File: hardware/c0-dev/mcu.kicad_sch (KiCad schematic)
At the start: 28 parts, among them J2 TAG_CONNECT, U7 W25Q128JVP, U8 RP2350A, Y1 ABM8-272-T3 (12Mhz)

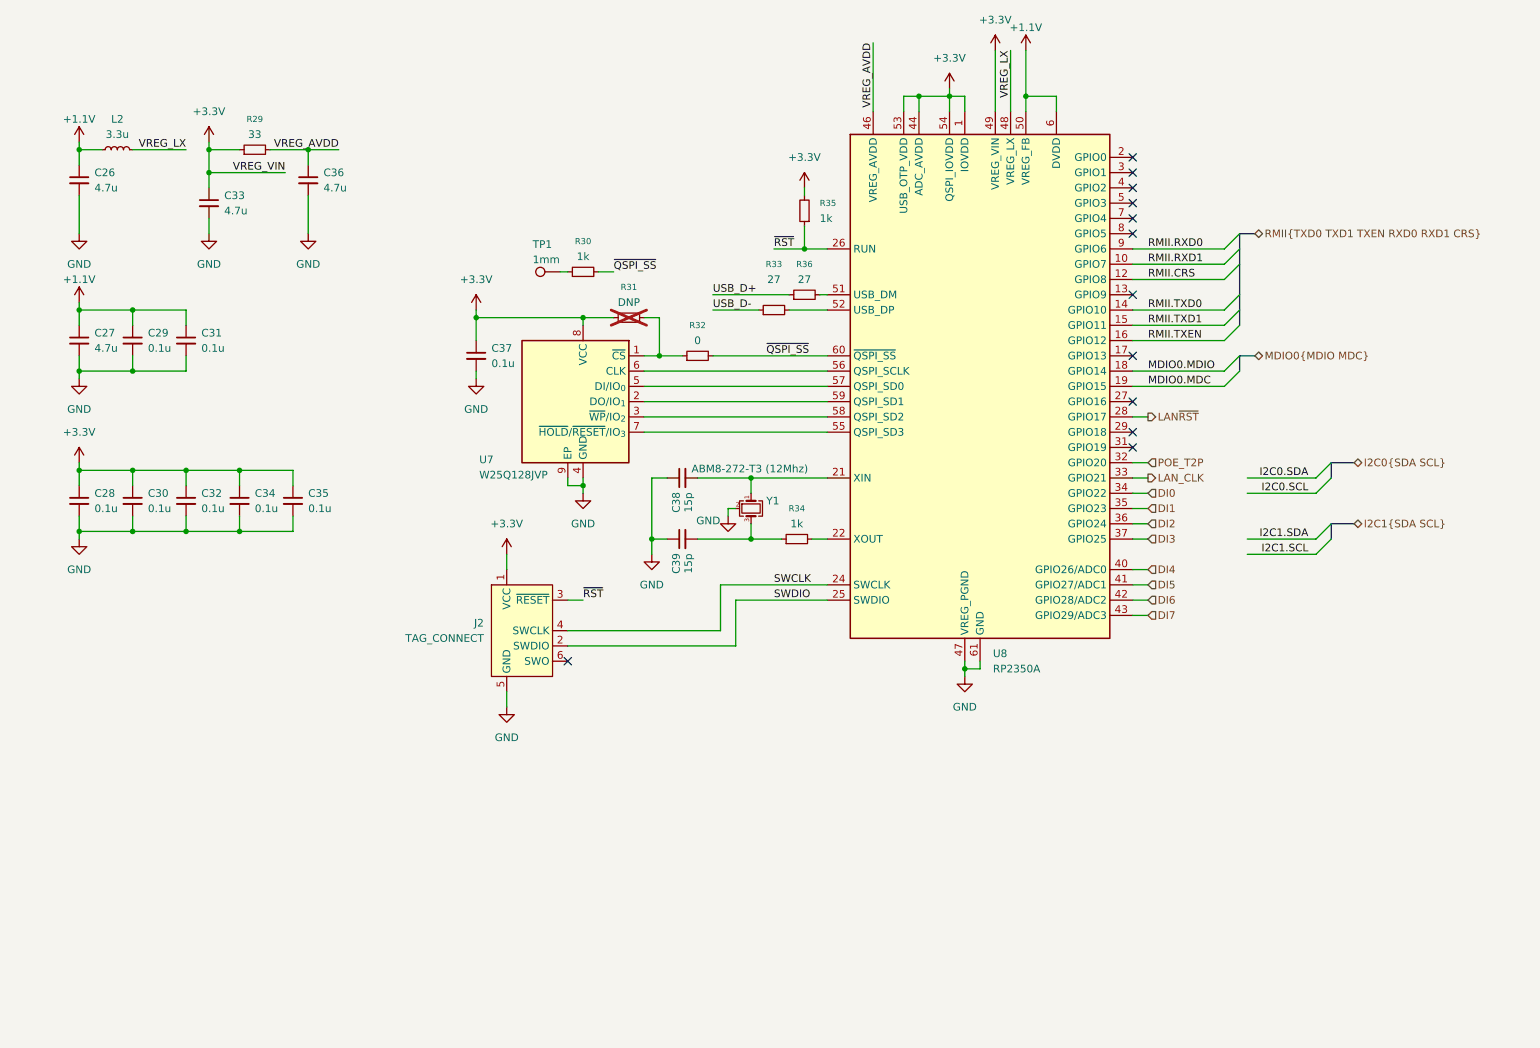
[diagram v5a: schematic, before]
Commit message: connections and i2c clock split
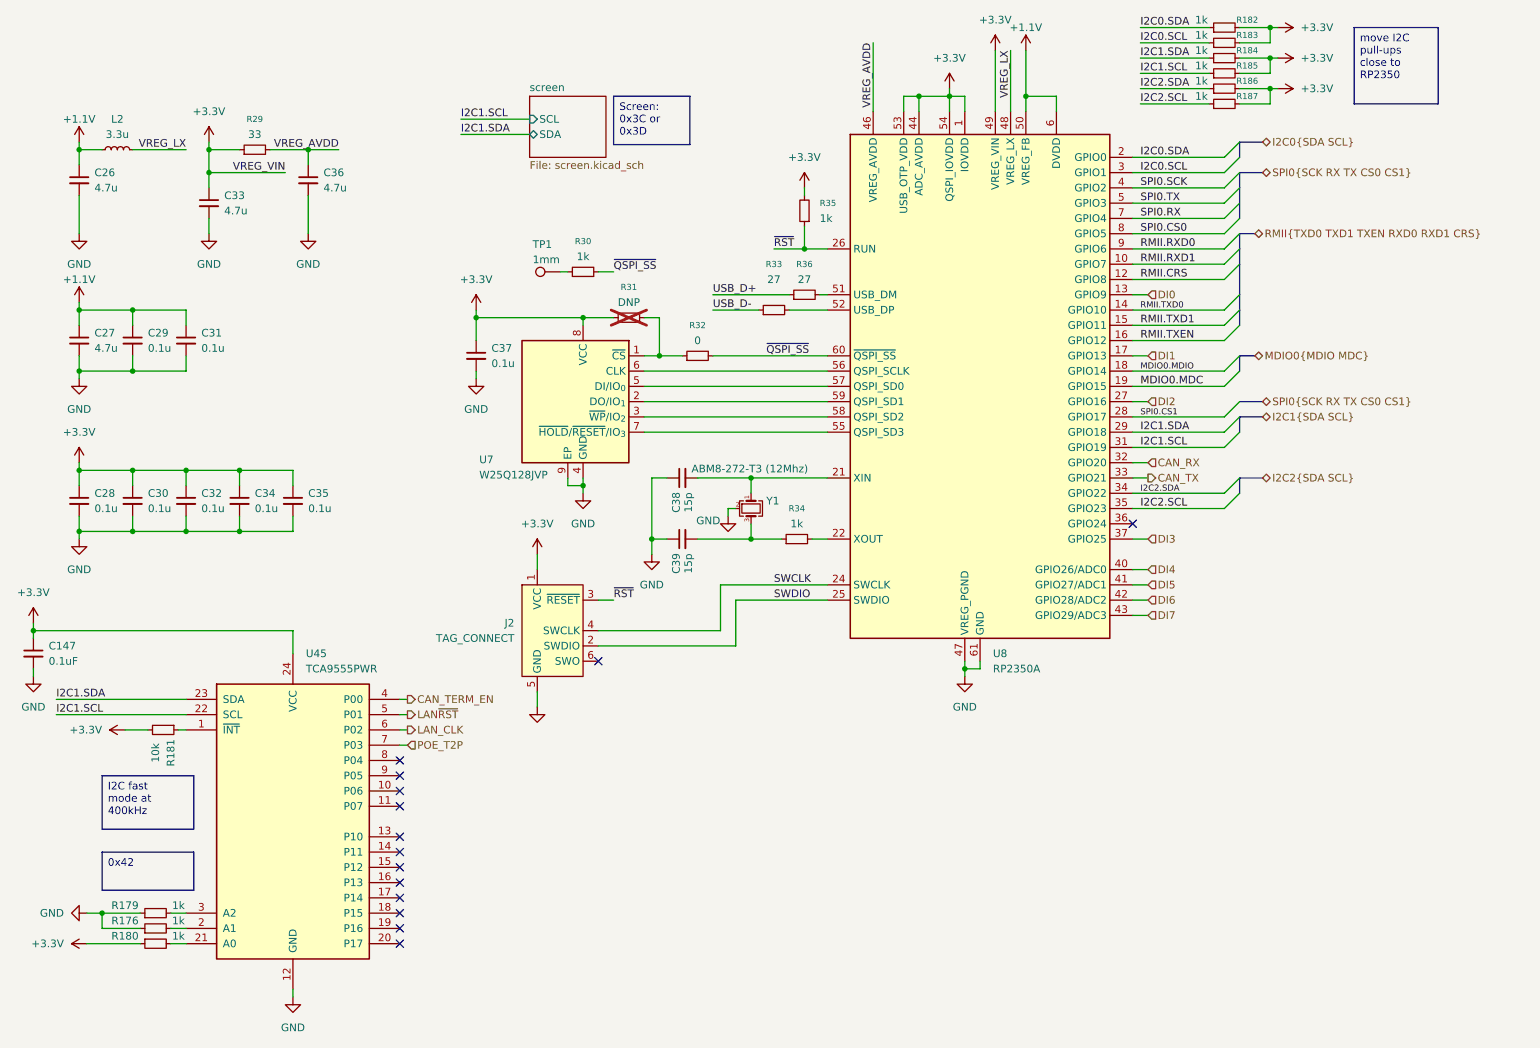
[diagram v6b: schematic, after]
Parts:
- added C147: 0.1uF, Capacitor_SMD:C_0402_1005Metric, symbol Device:C_Small
- added R176, R179, R180, R182, R183, R184, R185, R186, R187: 1k, Resistor_SMD:R_0402_1005Metric, symbol Device:R_Small
- added R181: 10k, Resistor_SMD:R_0402_1005Metric, symbol Device:R_Small
- added U45: TCA9555PWR, Package_SO:TSSOP-24_4.4x7.8mm_P0.65mm, symbol Interface_Expansion:TCA9555PWR
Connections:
- net +3.3V: now also C147.1, R180.1, R181.2, R182.2, R183.2, R184.2, R185.2, R186.2, R187.2, U45.24 (VCC)
- net DI0: now also U8.13 (GPIO9); no longer U8.34 (GPIO22)
- net DI1: now also U8.17 (GPIO13); no longer U8.35 (GPIO23)
- net DI2: now also U8.27 (GPIO16); no longer U8.36 (GPIO24)
- net GND: now also C147.2, R176.1, R179.1, U45.12 (GND)
- net I2C0.SCL: now also U8.3 (GPIO1), R183.1
- net I2C0.SDA: now also U8.2 (GPIO0), R182.1
- net I2C1.SCL: now also U8.31 (GPIO19), R185.1, U45.22 (SCL)
- net I2C1.SDA: now also U8.29 (GPIO18), R184.1, U45.23 (SDA)
- net LAN_CLK: now also U45.6 (P02); no longer U8.33 (GPIO21)
- net LAN~{RST}: now also U45.5 (P01); no longer U8.28 (GPIO17)
- net POE_T2P: now also U45.7 (P03); no longer U8.32 (GPIO20)
- net SPI0.SCK: now reaches U8.4 (GPIO2)
- net SPI0.TX: now reaches U8.5 (GPIO3)
- net SPI0.RX: now reaches U8.7 (GPIO4)
- net SPI0.CS0: now reaches U8.8 (GPIO5)
- new net: R181.1, U45.1 (~{INT})
- new net: R176.2, U45.2 (A1)
- new net: R180.2, U45.21 (A0)
- new net: R179.2, U45.3 (A2)
- new net CAN_RX: U8.32 (GPIO20)
- new net CAN_TERM_EN: U45.4 (P00)
- new net CAN_TX: U8.33 (GPIO21)
- new net I2C2.SCL: R187.1, U8.35 (GPIO23)
- new net I2C2.SDA: R186.1, U8.34 (GPIO22)
- new net SPI0.CS1: U8.28 (GPIO17)
- no-connect marks 12 -> 14
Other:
- added sheet screen (screen.kicad_sch)
- moved on the sheet: J2

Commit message: connector
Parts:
- added TP2, TP3: TestPoint, TestPoint:TestPoint_Pad_D2.0mm, symbol Connector:TestPoint
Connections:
- net USB_D+: now also TP2.1
- net USB_D-: now also TP3.1
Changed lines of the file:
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@@
 	(wire
 		(pts
+			(xy 259.08 135.89) (xy 259.08 139.7)
+		)
+		(stroke
+			(width 0)
+			(type default)
+		)
+	)
+	(wire
+		(pts
 			(xy 218.44 44.45) (xy 233.68 44.45)
 		)
@@
 	(wire
 		(pts
+			(xy 247.65 135.89) (xy 259.08 135.89)
+		)
+		(stroke
+			(width 0)
+			(type default)
+		)
+	)
+	(wire
+		(pts
 			(xy 58.42 175.26) (xy 60.96 175.26)
 		)
@@
 	(wire
 		(pts
+			(xy 247.65 133.35) (xy 260.35 133.35)
+		)
+		(stroke
+			(width 0)
+			(type default)
+		)
+	)
+	(wire
+		(pts
 			(xy 218.44 107.95) (xy 220.98 107.95)
 		)
@@
 	(wire
 		(pts
+			(xy 259.08 139.7) (xy 260.35 139.7)
+		)
+		(stroke
+			(width 0)
+			(type default)
+		)
+	)
+	(wire
+		(pts
 			(xy 64.77 41.91) (xy 64.77 43.18)
 		)
@@
 		)
 	)
+	(label "USB_D-"
+		(at 247.65 135.89 0)
+		(effects
+			(font
+				(size 1.27 1.27)
+			)
+			(justify left bottom)
+		)
+	)
 	(label "VREG_LX"
 		(at 60.96 43.18 180)
@@
 		)
 	)
+	(label "USB_D+"
+		(at 247.65 133.35 0)
+		(effects
+			(font
+				(size 1.27 1.27)
+			)
+			(justify left bottom)
+		)
+	)
 	(label "SPI0.TX"
 		(at 219.71 52.07 0)
@@
 	)
 	(symbol
+		(lib_id "Connector:TestPoint")
+		(at 260.35 139.7 270)
+		(unit 1)
+		(body_style 1)
+		(exclude_from_sim no)
+		(in_bom yes)
+		(on_board yes)
+		(in_pos_files yes)
+		(dnp no)
+		(fields_autoplaced yes)
+		(property "Reference" "TP3"
+			(at 265.43 138.4299 90)
+			(show_name no)
+			(do_not_autoplace no)
+			(effects
+				(font
+					(size 1.27 1.27)
+				)
+				(justify left)
+			)
+		)
+		(property "Value" "TestPoint"
+			(at 265.43 140.9699 90)
+			(show_name no)
+			(do_not_autoplace no)
+			(effects
+				(font
+					(size 1.27 1.27)
+				)
+				(justify left)
+			)
+		)
+		(property "Footprint" "TestPoint:TestPoint_Pad_D2.0mm"
+			(at 260.35 144.78 0)
+			(hide yes)
+			(show_name no)
+			(do_not_autoplace no)
+			(effects
+				(font
+					(size 1.27 1.27)
+				)
+			)
+		)
+		(property "Datasheet" ""
+			(at 260.35 144.78 0)
+			(hide yes)
+			(show_name no)
+			(do_not_autoplace no)
+			(effects
+				(font
+					(size 1.27 1.27)
+				)
+			)
+		)
+		(property "Description" "test point"
+			(at 260.35 139.7 0)
+			(hide yes)
+			(show_name no)
+			(do_not_autoplace no)
+			(effects
+				(font
+					(size 1.27 1.27)
+				)
+			)
+		)
+		(pin "1"
+		)
+		(instances
+			(project "c0-dev"
+				(path "/b8347a0e-ad04-4414-969d-3c64a611d74e/b3a362d3-bb15-48bf-a1e5-1773c27a02b7"
+					(reference "TP3")
+					(unit 1)
+				)
+			)
+		)
+	)
+	(symbol
 		(lib_id "Device:C_Small")
 		(at 35.56 127 0)
@@
 					(unit 1)
 				)
+			)
+		)
+	)
+	(symbol
+		(lib_id "Connector:TestPoint")
+		(at 260.35 133.35 270)
+		(unit 1)
+		(body_style 1)
+		(exclude_from_sim no)
+		(in_bom yes)
+		(on_board yes)
+		(in_pos_files yes)
+		(dnp no)
+		(fields_autoplaced yes)
+		(property "Reference" "TP2"
+			(at 265.43 132.0799 90)
+			(show_name no)
+			(do_not_autoplace no)
+			(effects
+				(font
+					(size 1.27 1.27)
+				)
+				(justify left)
+			)
+		)
+		(property "Value" "TestPoint"
+			(at 265.43 134.6199 90)
+			(show_name no)
+			(do_not_autoplace no)
+			(effects
+				(font
+					(size 1.27 1.27)
+				)
+				(justify left)
+			)
+		)
+		(property "Footprint" "TestPoint:TestPoint_Pad_D2.0mm"
+			(at 260.35 138.43 0)
+			(hide yes)
+			(show_name no)
+			(do_not_autoplace no)
+			(effects
+				(font
+					(size 1.27 1.27)
+				)
+			)
+		)
+		(property "Datasheet" ""
+			(at 260.35 138.43 0)
+			(hide yes)
+			(show_name no)
+			(do_not_autoplace no)
+			(effects
+				(font
+					(size 1.27 1.27)
+				)
+			)
+		)
+		(property "Description" "test point"
+			(at 260.35 133.35 0)
+			(hide yes)
+			(show_name no)
+			(do_not_autoplace no)
+			(effects
+				(font
+					(size 1.27 1.27)
+				)
+			)
+		)
+		(pin "1"
+		)
+		(instances
+			(project "c0-dev"
+				(path "/b8347a0e-ad04-4414-969d-3c64a611d74e/b3a362d3-bb15-48bf-a1e5-1773c27a02b7"
+					(reference "TP2")
+					(unit 1)
+				)

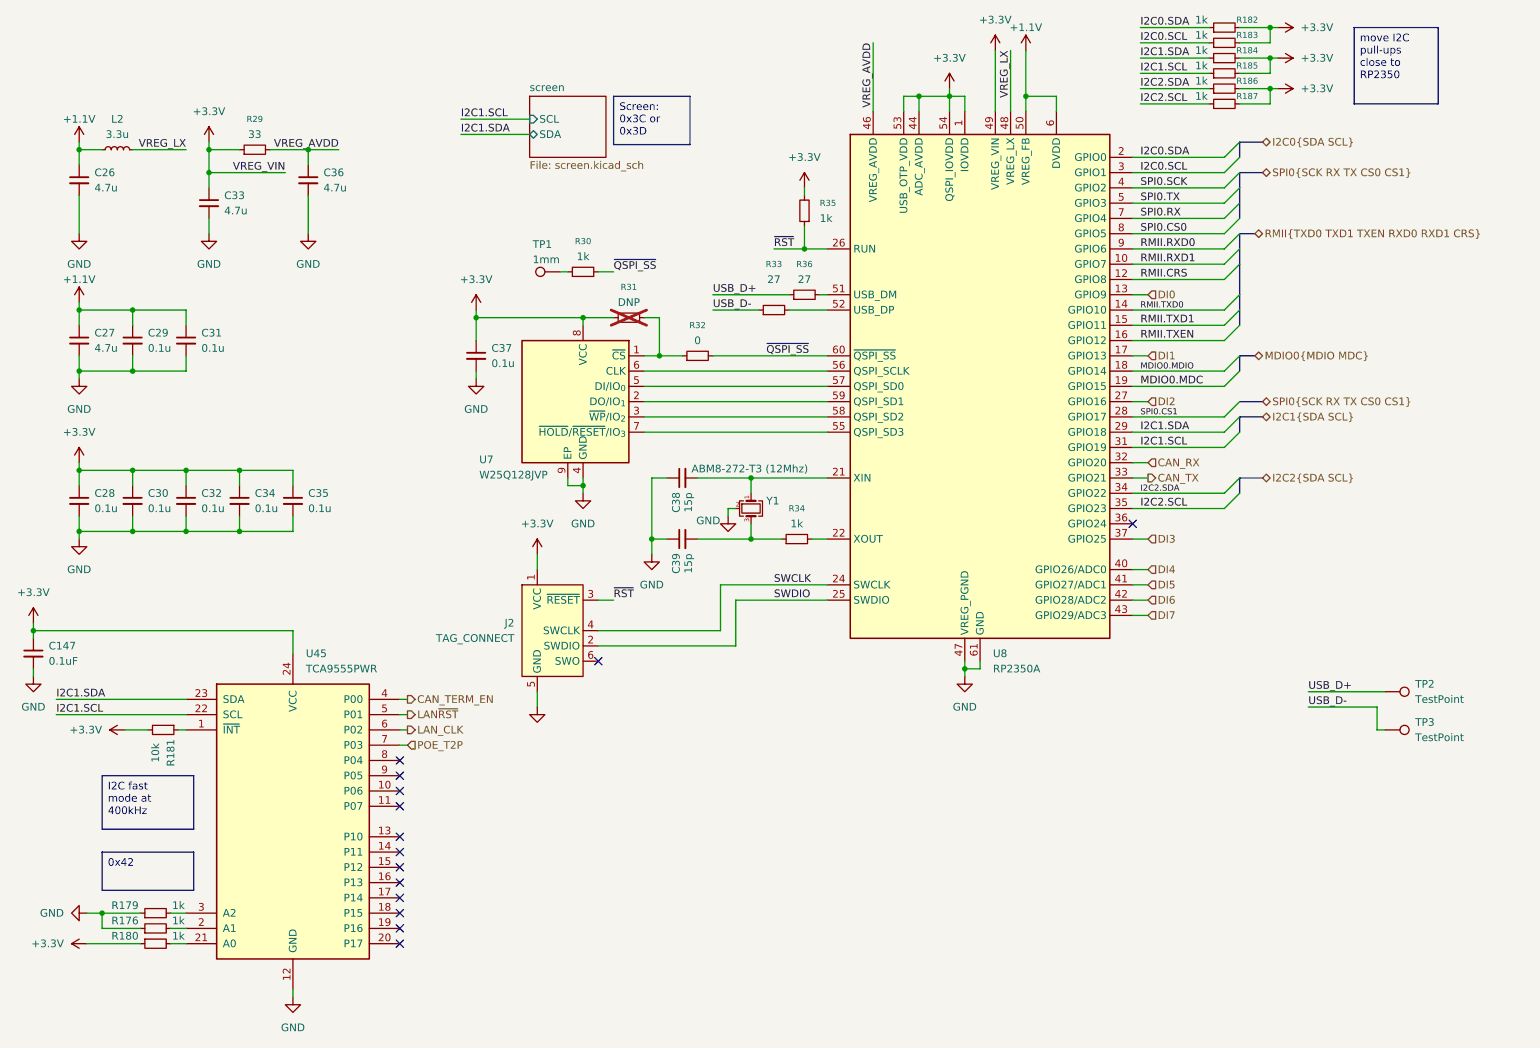
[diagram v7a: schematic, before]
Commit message: added connectors
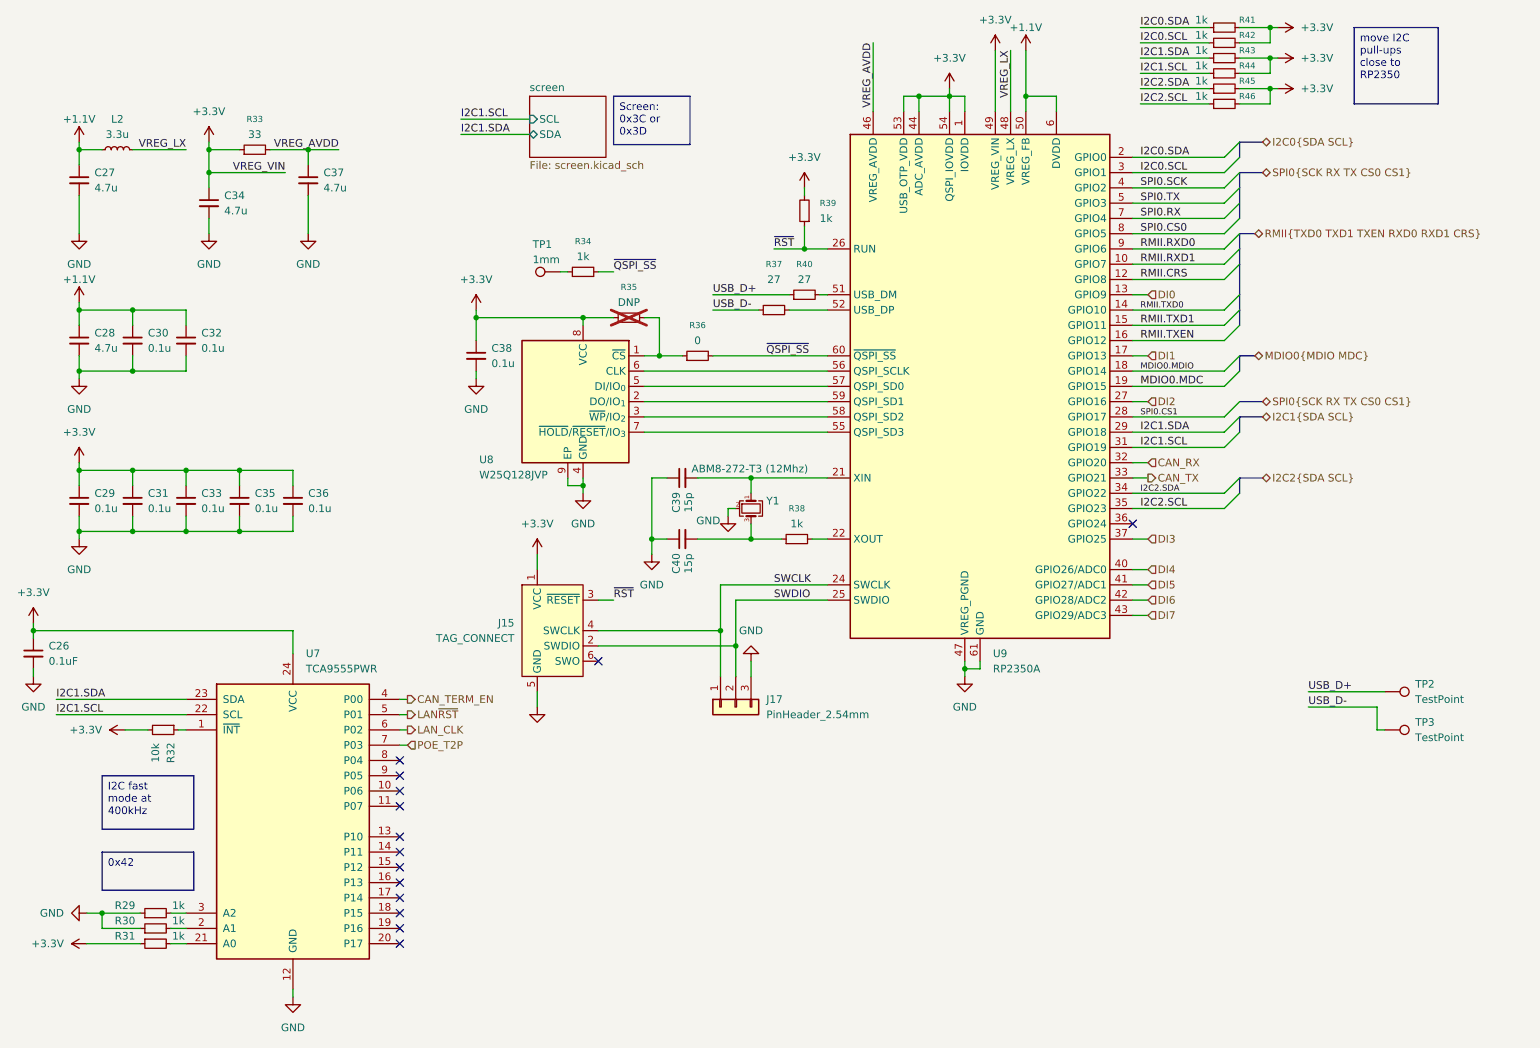
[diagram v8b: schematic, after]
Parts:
- added J17: PinHeader_2.54mm, Connector_PinHeader_2.54mm:PinHeader_1x03_P2.54mm_Vertical_SMD_Pin1Left, symbol Connector_Generic:Conn_01x03
- renumbered C147 to C26, C26 to C27, C27 to C28, C28 to C29, C29 to C30, C30 to C31, C31 to C32, C32 to C33, C33 to C34, C34 to C35, C35 to C36, C36 to C37, C37 to C38, C38 to C39, C39 to C40, J2 to J15, R179 to R29, R176 to R30, R180 to R31, R181 to R32, R29 to R33, R30 to R34, R31 to R35, R32 to R36, R33 to R37, R34 to R38, R35 to R39, R36 to R40, R182 to R41, R183 to R42, R184 to R43, R185 to R44, R186 to R45, R187 to R46, U45 to U7, U7 to U8, U8 to U9
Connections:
- net GND: now also J17.3 (Pin_3)
- net SWCLK: now also J17.1 (Pin_1)
- net SWDIO: now also J17.2 (Pin_2)
